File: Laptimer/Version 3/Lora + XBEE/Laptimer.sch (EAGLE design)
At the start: 70 parts, among them IC1 MCP73831/OT, IC2 REG1117, Q1 8mhz, Q4 PBSS4120T, U2 LTC3872ETS8TRMPBF, U3 SI3460DDV-T1-GE3, X1 mini-usb

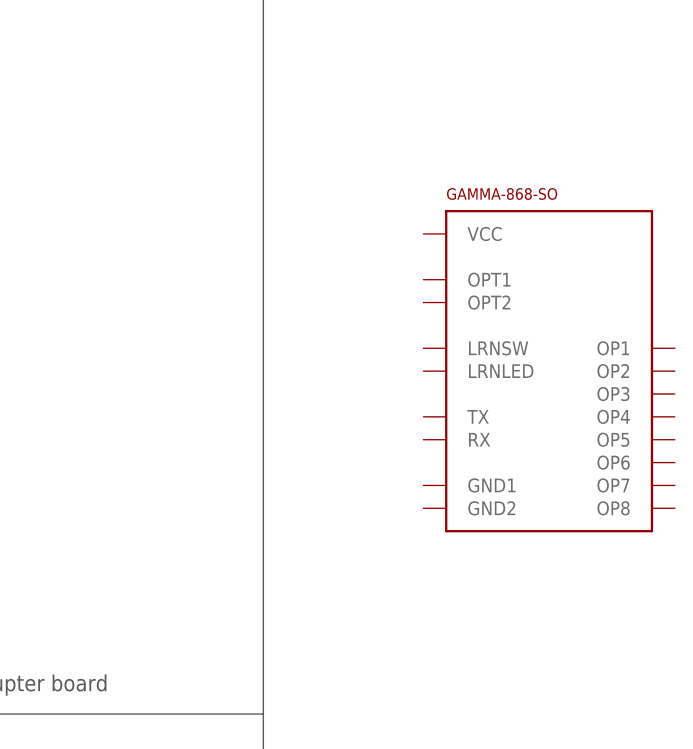
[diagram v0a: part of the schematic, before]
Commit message: com node board size to small, working on bigger
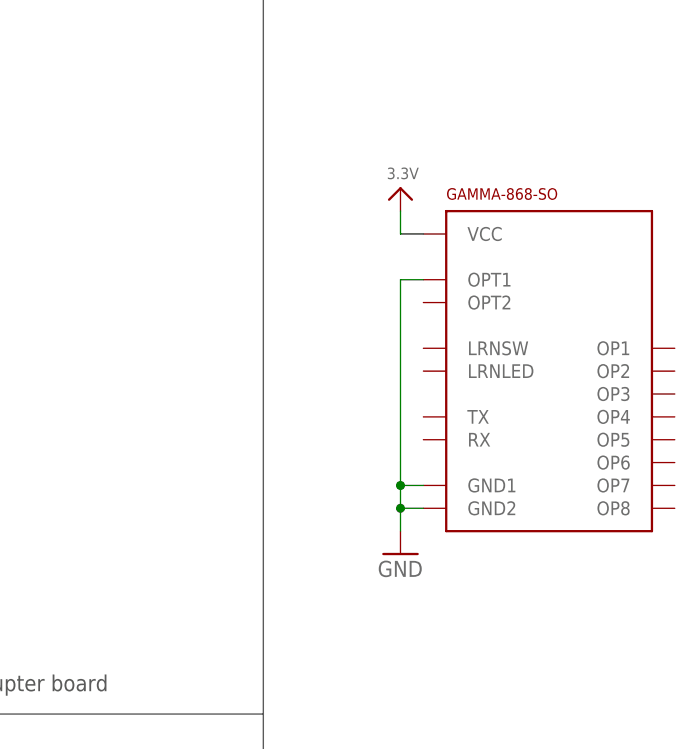
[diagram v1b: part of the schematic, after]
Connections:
- net 3.3V: now also U$7.VCC
- net GND: now also U$7.GND1, U$7.GND2, U$7.OPT1
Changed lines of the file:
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@@
 <part name="R5" library="microbuilder" deviceset="RESISTOR" device="_0603" value="1k"/>
 <part name="Q4" library="microbuilder" deviceset="TRANSISTOR_NPN" device="WIDE" value="PBSS4120T"/>
+<part name="U$1" library="microbuilder" deviceset="3.3V" device=""/>
+<part name="GND13" library="supply1" deviceset="GND" device=""/>
 </parts>
 <sheets>
@@
 <instance part="R5" gate="G$1" x="71.12" y="213.36" rot="R270"/>
 <instance part="Q4" gate="G$1" x="83.82" y="223.52"/>
+<instance part="U$1" gate="G$1" x="215.9" y="104.14"/>
+<instance part="GND13" gate="1" x="215.9" y="63.5"/>
 </instances>
 <busses>
@@
 <pinref part="C14" gate="G$1" pin="P$2"/>
 </segment>
+<segment>
+<pinref part="U$7" gate="G$1" pin="OPT1"/>
+<pinref part="GND13" gate="1" pin="GND"/>
+<wire x1="218.44" y1="93.98" x2="215.9" y2="93.98" width="0.1524" layer="91"/>
+<wire x1="215.9" y1="93.98" x2="215.9" y2="71.12" width="0.1524" layer="91"/>
+<pinref part="U$7" gate="G$1" pin="GND1"/>
+<wire x1="215.9" y1="71.12" x2="215.9" y2="68.58" width="0.1524" layer="91"/>
+<wire x1="215.9" y1="68.58" x2="215.9" y2="66.04" width="0.1524" layer="91"/>
+<wire x1="218.44" y1="71.12" x2="215.9" y2="71.12" width="0.1524" layer="91"/>
+<junction x="215.9" y="71.12"/>
+<pinref part="U$7" gate="G$1" pin="GND2"/>
+<wire x1="218.44" y1="68.58" x2="215.9" y2="68.58" width="0.1524" layer="91"/>
+<junction x="215.9" y="68.58"/>
+</segment>
 </net>
 <net name="XTAL2" class="0">
@@
 <pinref part="U$10" gate="G$1" pin="3.3V"/>
 </segment>
-</net>
+<segment>
+<pinref part="U$7" gate="G$1" pin="VCC"/>
+<pinref part="U$1" gate="G$1" pin="3.3V"/>
+<wire x1="218.44" y1="99.06" x2="215.9" y2="99.06" width="0.1524" layer="91"/>
+<wire x1="215.9" y1="99.06" x2="215.9" y2="101.6" width="0.1524" layer="91"/>
+</segment>
+</net>

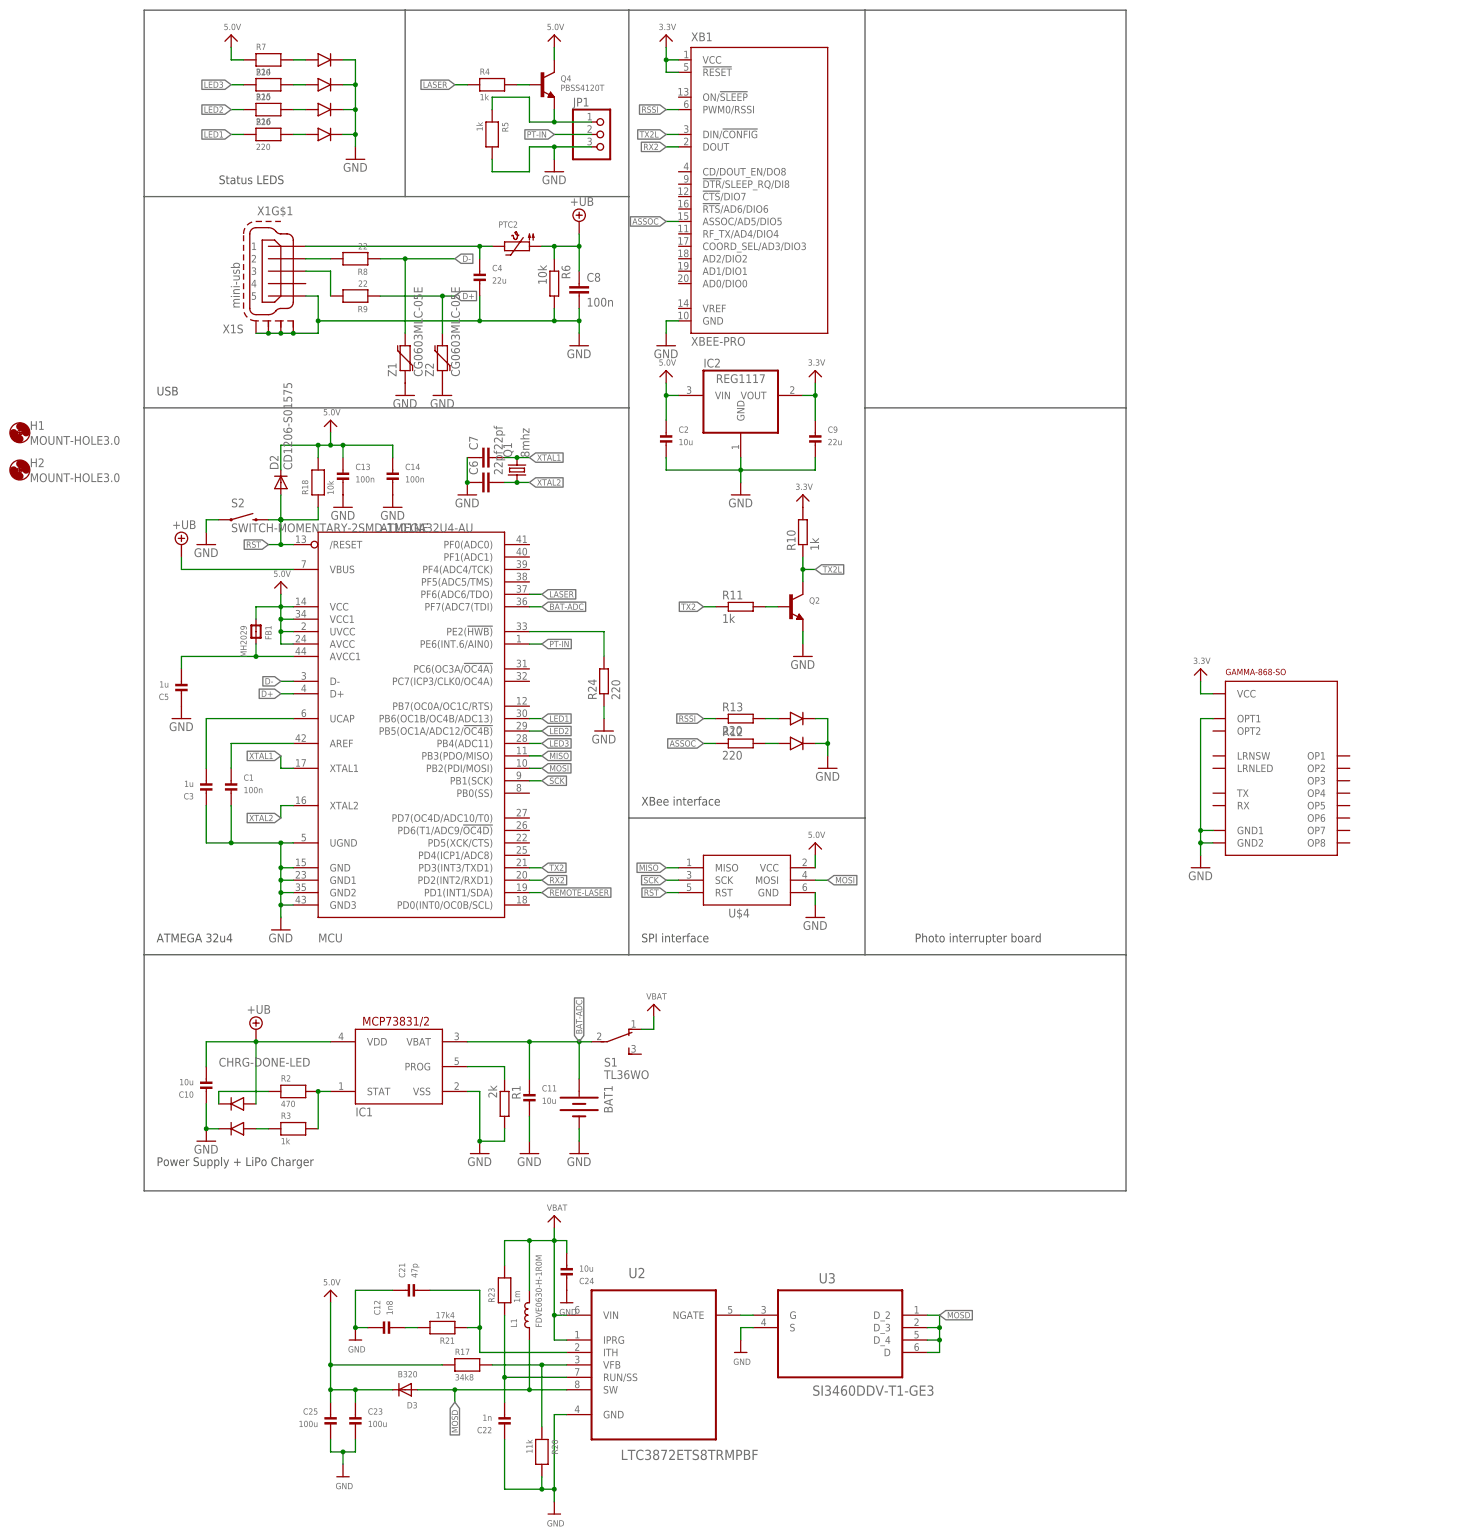
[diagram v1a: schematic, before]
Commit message: laptimer RC done, com node (done) need checkup
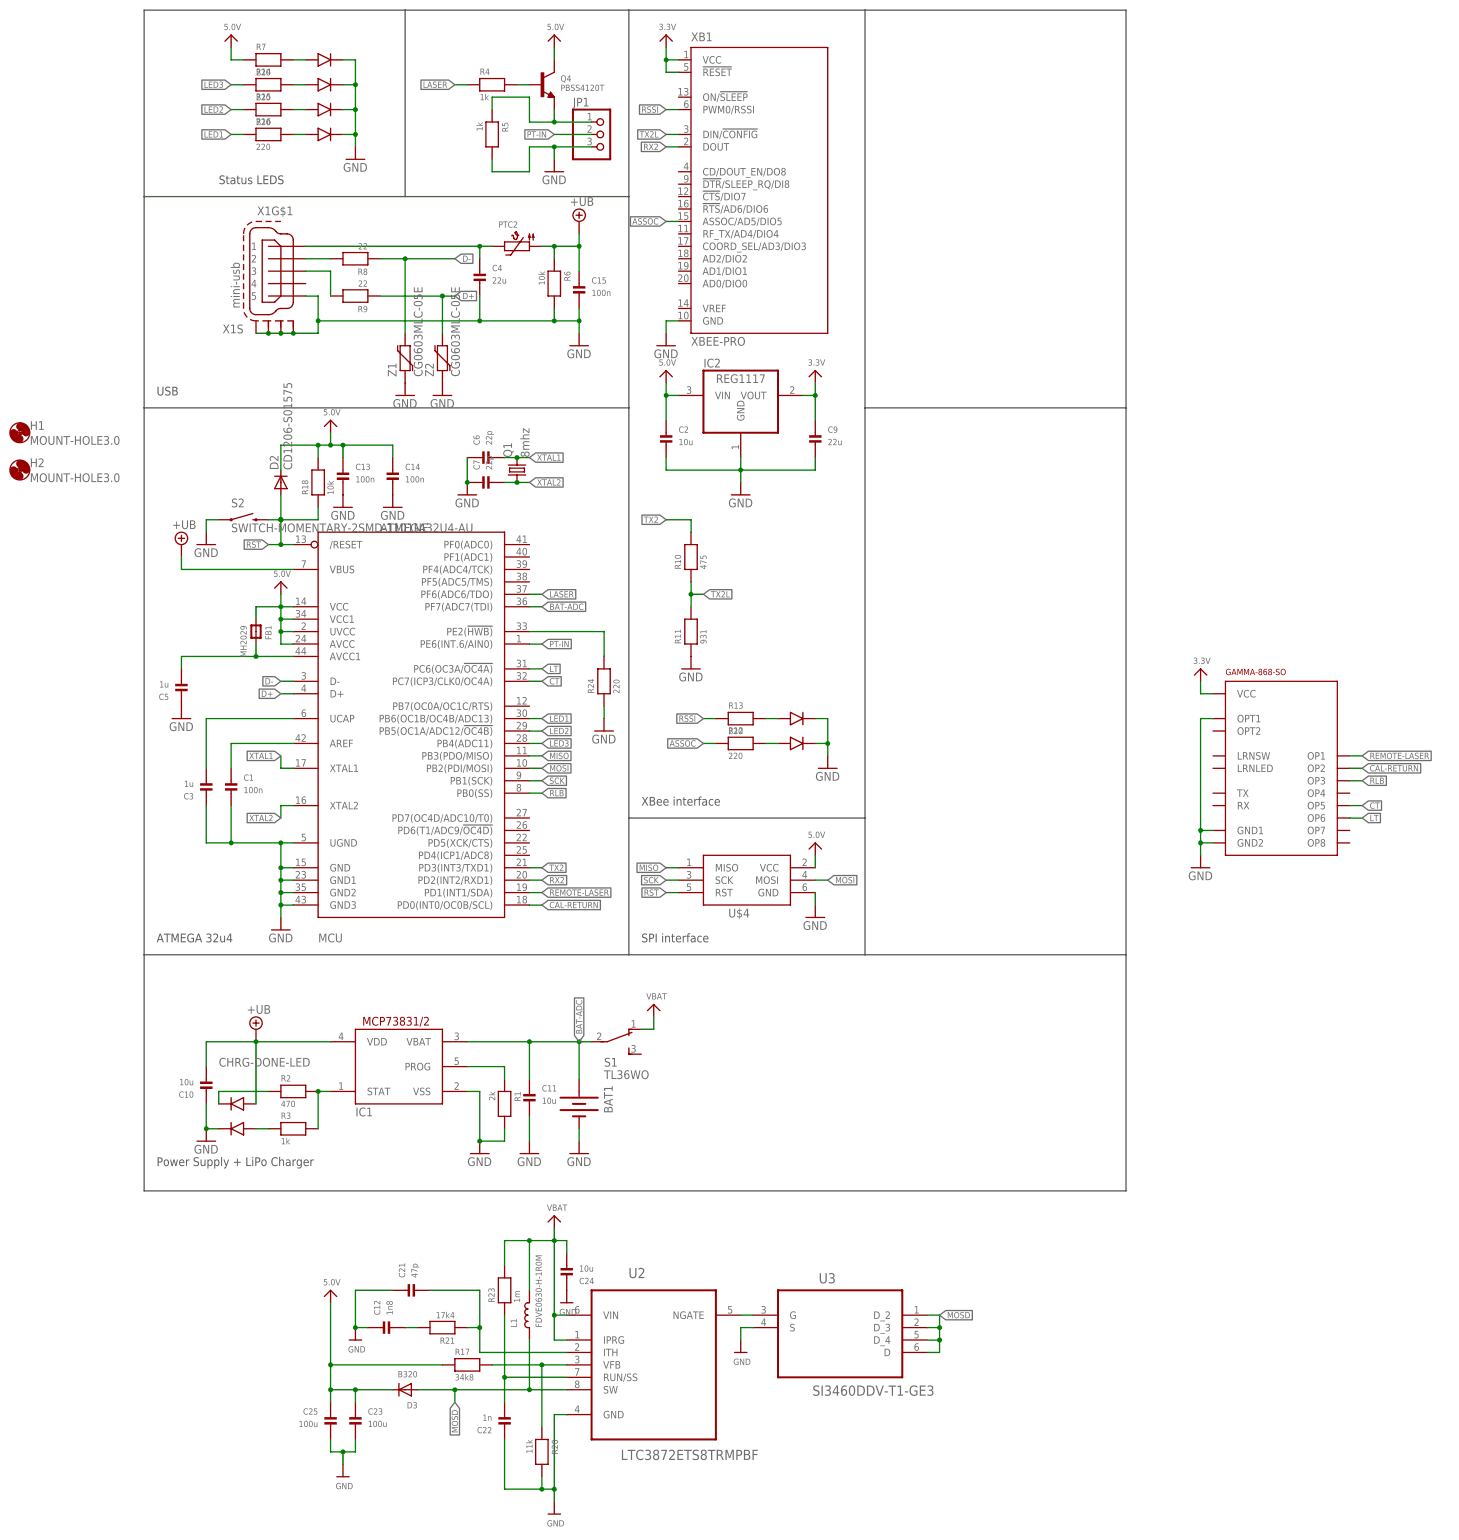
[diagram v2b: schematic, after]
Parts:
- removed C8: 100n, rcl:C-EUC0603K
- removed Q2: (no value), microbuilder:TRANSISTOR_NPNWIDE
- added C15: 100n, microbuilder:CAP_CERAMIC_0603
- C10, C11: device microbuilder:CAP_CERAMIC_0805MP -> microbuilder:CAP_CERAMIC_0805
- C6, C7: value 22pf -> 22p; device rcl:C-EUC0603K -> microbuilder:CAP_CERAMIC_0603
- R1, R12, R13, R24, R6: device rcl:R-EU_R0603 -> microbuilder:RESISTOR_0603
- R10: value 1k -> 475; device rcl:R-EU_R0603 -> microbuilder:RESISTOR_0603
- R11: value 1k -> 931; device rcl:R-EU_R0603 -> microbuilder:RESISTOR_0603
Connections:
- removed net N$18: Q2.B, R11.2
- new net CAL-RETURN: MCU.PD0(INT0/OC0B/SCL), U$7.OP2
- new net CT: MCU.PC7(ICP3/CLK0/OC4A), U$7.OP5
- new net LT: MCU.PC6(OC3A/!OC4A), U$7.OP6
- new net RLB: MCU.PB0(SS), U$7.OP3
- net +UB: now also C15.P$1; no longer C8.1
- net 3.3V: no longer R10.2
- net GND: now also C15.P$2, C6.P$1, C7.P$1, R11.1; no longer C6.1, C7.1, C8.2, Q2.E
- net REMOTE-LASER: now also U$7.OP1
- net TX2: now also R10.2; no longer R11.1
- net TX2L: now also R11.2; no longer Q2.C
- net XTAL1: now also C6.P$2; no longer C7.2
- net XTAL2: now also C7.P$2; no longer C6.2
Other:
- note removed: "Photo interrupter board"
- moved on the sheet: C6, C7, R10, R11
